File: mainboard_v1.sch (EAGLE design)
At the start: 16 parts

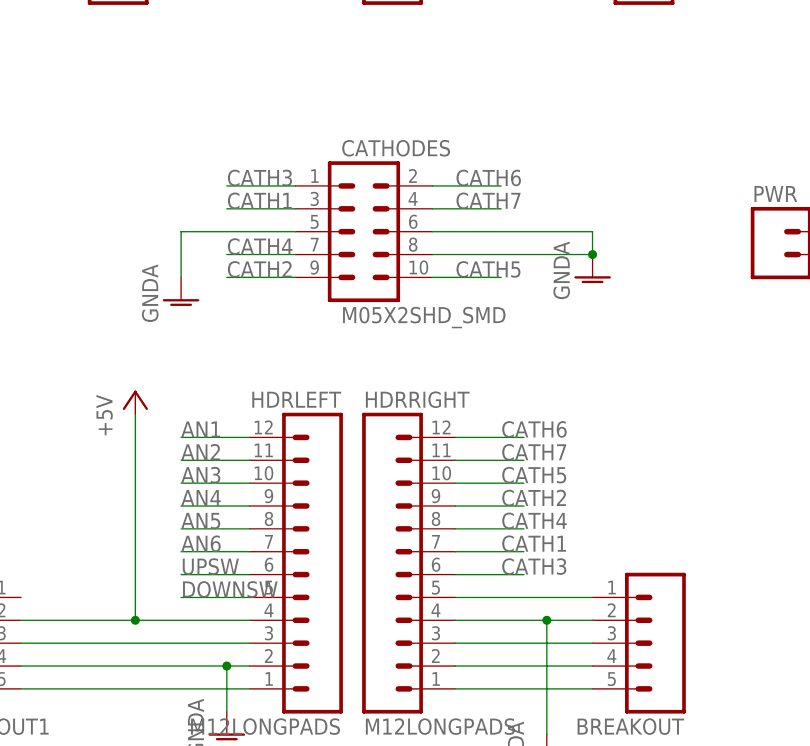
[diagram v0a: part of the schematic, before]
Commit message: add labels to boards to aid in, you know, using them
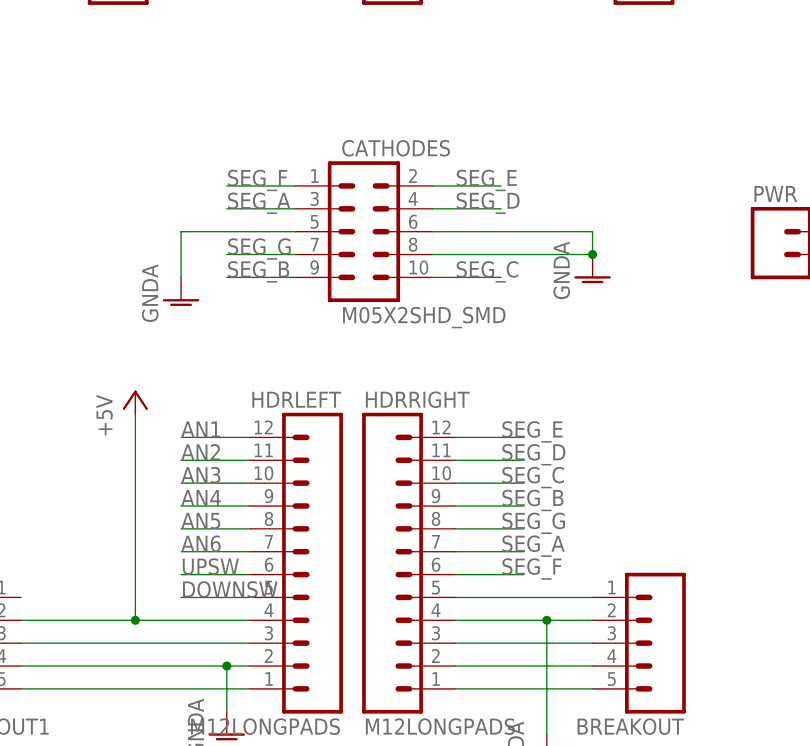
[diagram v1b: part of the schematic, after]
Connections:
- net CATH1 renamed SEG_A
- net CATH2 renamed SEG_B
- net CATH3 renamed SEG_F
- net CATH4 renamed SEG_G
- net CATH5 renamed SEG_C
- net CATH6 renamed SEG_E
- net CATH7 renamed SEG_D
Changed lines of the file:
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@@
 </segment>
 </net>
-<net name="CATH7" class="0">
+<net name="SEG_D" class="0">
 <segment>
 <pinref part="CATHODES" gate="G$1" pin="4"/>
@@
 </segment>
 </net>
-<net name="CATH6" class="0">
+<net name="SEG_E" class="0">
 <segment>
 <pinref part="CATHODES" gate="G$1" pin="2"/>
@@
 </segment>
 </net>
-<net name="CATH5" class="0">
+<net name="SEG_C" class="0">
 <segment>
 <pinref part="HDRRIGHT" gate="G$1" pin="10"/>
@@
 </segment>
 </net>
-<net name="CATH4" class="0">
+<net name="SEG_G" class="0">
 <segment>
 <pinref part="CATHODES" gate="G$1" pin="7"/>
@@
 </segment>
 </net>
-<net name="CATH3" class="0">
+<net name="SEG_F" class="0">
 <segment>
 <pinref part="CATHODES" gate="G$1" pin="1"/>
@@
 </segment>
 </net>
-<net name="CATH2" class="0">
+<net name="SEG_B" class="0">
 <segment>
 <pinref part="CATHODES" gate="G$1" pin="9"/>
@@
 </segment>
 </net>
-<net name="CATH1" class="0">
+<net name="SEG_A" class="0">
 <segment>
 <pinref part="CATHODES" gate="G$1" pin="3"/>
